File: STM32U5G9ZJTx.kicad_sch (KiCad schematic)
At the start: 42 parts, among them J1 Conn_ST_STDC14, SW1 SW_Push, SW2 SW_Push, U1 STM32U5G9ZJTxQ, Y1 16MHz, Y2 32.768KHz

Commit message: layouting component to PCB
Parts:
- C1, C10, C11, C14, C16, C18, C19, C2, C20, C21, C23, C24, C25, C26, C29, C3, C30, C31, C32, C33, C4, C5, C6, C7, C8, C9: footprint (none) -> Capacitor_SMD:C_0402_1005Metric
- C12, C13, C15, C17, C22, C27, C28: footprint (none) -> Capacitor_SMD:C_0603_1608Metric
- J1: footprint (none) -> Connector_PinHeader_1.27mm:PinHeader_2x07_P1.27mm_Vertical_SMD
- L1: footprint (none) -> Inductor_SMD:L_0603_1608Metric
- R1: footprint (none) -> Resistor_SMD:R_0402_1005Metric
- SW1, SW2: footprint (none) -> Button_Switch_SMD:SW_SPST_PTS810
- Y1: footprint (none) -> Crystal:Crystal_SMD_2520-4Pin_2.5x2.0mm
- Y2: footprint (none) -> Crystal:Crystal_SMD_2012-2Pin_2.0x1.2mm
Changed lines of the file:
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@@
 		(polyline
 			(pts
-				(xy 240.03 144.78) (xy 265.43 144.78) (xy 265.43 119.38) (xy 240.03 119.38)
+				(xy 299.72 203.2) (xy 299.72 224.79) (xy 316.23 224.79) (xy 316.23 203.2)
 			)
 			(stroke
@@
 		(polyline
 			(pts
-				(xy 364.49 119.38) (xy 364.49 144.78) (xy 400.05 144.78) (xy 400.05 119.38)
+				(xy 293.37 154.94) (xy 341.63 154.94) (xy 341.63 186.69) (xy 293.37 186.69)
 			)
 			(stroke
@@
 		(polyline
 			(pts
-				(xy 240.03 78.74) (xy 381 78.74) (xy 381 52.07) (xy 240.03 52.07)
+				(xy 240.03 110.49) (xy 265.43 110.49) (xy 265.43 85.09) (xy 240.03 85.09)
 			)
 			(stroke
@@
 		(polyline
 			(pts
-				(xy 240.03 154.94) (xy 285.75 154.94) (xy 285.75 186.69) (xy 240.03 186.69)
+				(xy 364.49 119.38) (xy 364.49 144.78) (xy 400.05 144.78) (xy 400.05 119.38)
 			)
 			(stroke
@@
 		(polyline
 			(pts
-				(xy 240.03 110.49) (xy 265.43 110.49) (xy 265.43 85.09) (xy 240.03 85.09)
+				(xy 313.69 119.38) (xy 313.69 144.78) (xy 360.68 144.78) (xy 360.68 119.38)
 			)
 			(stroke
@@
 		(polyline
 			(pts
-				(xy 358.14 110.49) (xy 386.08 110.49) (xy 386.08 85.09) (xy 358.14 85.09)
+				(xy 240.03 154.94) (xy 285.75 154.94) (xy 285.75 186.69) (xy 240.03 186.69)
 			)
 			(stroke
@@
 		(polyline
 			(pts
-				(xy 299.72 203.2) (xy 299.72 224.79) (xy 316.23 224.79) (xy 316.23 203.2)
+				(xy 313.69 110.49) (xy 349.25 110.49) (xy 349.25 85.09) (xy 313.69 85.09)
 			)
 			(stroke
@@
 		(polyline
 			(pts
-				(xy 313.69 119.38) (xy 313.69 144.78) (xy 360.68 144.78) (xy 360.68 119.38)
+				(xy 240.03 44.45) (xy 276.86 44.45) (xy 276.86 16.51) (xy 240.03 16.51)
 			)
 			(stroke
@@
 		(polyline
 			(pts
-				(xy 274.32 110.49) (xy 304.8 110.49) (xy 304.8 85.09) (xy 274.32 85.09)
+				(xy 304.8 144.78) (xy 304.8 119.38) (xy 274.32 119.38) (xy 274.32 144.78)
 			)
 			(stroke
@@
 		(polyline
 			(pts
-				(xy 304.8 144.78) (xy 304.8 119.38) (xy 274.32 119.38) (xy 274.32 144.78)
+				(xy 274.32 110.49) (xy 304.8 110.49) (xy 304.8 85.09) (xy 274.32 85.09)
 			)
 			(stroke
@@
 		(polyline
 			(pts
-				(xy 313.69 110.49) (xy 349.25 110.49) (xy 349.25 85.09) (xy 313.69 85.09)
+				(xy 240.03 78.74) (xy 381 78.74) (xy 381 52.07) (xy 240.03 52.07)
 			)
 			(stroke
@@
 		(polyline
 			(pts
-				(xy 293.37 154.94) (xy 341.63 154.94) (xy 341.63 186.69) (xy 293.37 186.69)
+				(xy 240.03 144.78) (xy 265.43 144.78) (xy 265.43 119.38) (xy 240.03 119.38)
 			)
 			(stroke
@@
 		(polyline
 			(pts
-				(xy 240.03 44.45) (xy 276.86 44.45) (xy 276.86 16.51) (xy 240.03 16.51)
+				(xy 358.14 110.49) (xy 386.08 110.49) (xy 386.08 85.09) (xy 358.14 85.09)
 			)
 			(stroke
@@
 			)
 		)
-		(property "Footprint" ""
+		(property "Footprint" "Capacitor_SMD:C_0402_1005Metric"
 			(at 257.81 173.99 0)
 			(effects
@@
 			)
 		)
-		(property "Footprint" ""
+		(property "Footprint" "Capacitor_SMD:C_0402_1005Metric"
 			(at 256.54 132.08 0)
 			(effects
@@
 			)
 		)
-		(property "Footprint" ""
+		(property "Footprint" "Capacitor_SMD:C_0603_1608Metric"
 			(at 321.0052 101.6 0)
 			(effects
@@
 			)
 		)
-		(property "Footprint" ""
+		(property "Footprint" "Capacitor_SMD:C_0603_1608Metric"
 			(at 246.0752 69.85 0)
 			(effects
@@
 			)
 		)
-		(property "Footprint" ""
+		(property "Footprint" "Button_Switch_SMD:SW_SPST_PTS810"
 			(at 367.03 201.93 0)
 			(effects
@@
 			)
 		)
-		(property "Footprint" ""
+		(property "Footprint" "Capacitor_SMD:C_0603_1608Metric"
 			(at 338.7852 137.16 0)
 			(effects
@@
 			)
 		)
-		(property "Footprint" ""
+		(property "Footprint" "Inductor_SMD:L_0603_1608Metric"
 			(at 328.93 128.27 0)
 			(effects
@@
 			)
 		)
-		(property "Footprint" ""
+		(property "Footprint" "Capacitor_SMD:C_0402_1005Metric"
 			(at 279.4 66.04 0)
 			(effects
@@
 			)
 		)
-		(property "Footprint" ""
+		(property "Footprint" "Capacitor_SMD:C_0402_1005Metric"
 			(at 267.97 31.75 0)
 			(effects
@@
 			)
 		)
-		(property "Footprint" ""
+		(property "Footprint" "Capacitor_SMD:C_0603_1608Metric"
 			(at 351.4852 137.16 0)
 			(effects
@@
 			)
 		)
-		(property "Footprint" ""
+		(property "Footprint" "Capacitor_SMD:C_0402_1005Metric"
 			(at 306.07 212.09 0)
 			(effects
@@
 			)
 		)
-		(property "Footprint" ""
+		(property "Footprint" "Capacitor_SMD:C_0402_1005Metric"
 			(at 302.26 66.04 0)
 			(effects
@@
 			)
 		)
-		(property "Footprint" ""
+		(property "Footprint" "Resistor_SMD:R_0402_1005Metric"
 			(at 359.41 213.36 0)
 			(effects
@@
 			)
 		)
-		(property "Footprint" ""
+		(property "Footprint" "Capacitor_SMD:C_0603_1608Metric"
 			(at 246.0752 35.56 0)
 			(effects
@@
 			)
 		)
-		(property "Footprint" ""
+		(property "Footprint" "Crystal:Crystal_SMD_2012-2Pin_2.0x1.2mm"
 			(at 317.5 167.64 0)
 			(effects
@@
 			)
 		)
-		(property "Footprint" ""
+		(property "Footprint" "Capacitor_SMD:C_0402_1005Metric"
 			(at 336.55 66.04 0)
 			(effects
@@
 			)
 		)
-		(property "Footprint" ""
+		(property "Footprint" "Capacitor_SMD:C_0402_1005Metric"
 			(at 382.27 133.35 0)
 			(effects
@@
 			)
 		)
-		(property "Footprint" ""
+		(property "Footprint" "Capacitor_SMD:C_0402_1005Metric"
 			(at 290.83 66.04 0)
 			(effects
@@
 			)
 		)
-		(property "Footprint" ""
+		(property "Footprint" "Capacitor_SMD:C_0402_1005Metric"
 			(at 313.69 66.04 0)
 			(effects
@@
 			)
 		)
-		(property "Footprint" ""
+		(property "Footprint" "Capacitor_SMD:C_0603_1608Metric"
 			(at 280.3652 137.16 0)
 			(effects
@@
 			)
 		)
-		(property "Footprint" ""
+		(property "Footprint" "Capacitor_SMD:C_0402_1005Metric"
 			(at 347.98 66.04 0)
 			(effects
@@
 			)
 		)
-		(property "Footprint" ""
+		(property "Footprint" "Capacitor_SMD:C_0402_1005Metric"
 			(at 256.54 66.04 0)
 			(effects
@@
 			)
 		)
-		(property "Footprint" ""
+		(property "Footprint" "Connector_PinHeader_1.27mm:PinHeader_2x07_P1.27mm_Vertical_SMD"
 			(at 270.51 219.71 0)
 			(effects
@@
 			)
 		)
-		(property "Footprint" ""
+		(property "Footprint" "Capacitor_SMD:C_0402_1005Metric"
 			(at 245.11 97.79 0)
 			(effects
@@
 			)
 		)
-		(property "Footprint" ""
+		(property "Footprint" "Capacitor_SMD:C_0402_1005Metric"
 			(at 322.58 171.45 0)
 			(effects
@@
 			)
 		)
-		(property "Footprint" ""
+		(property "Footprint" "Capacitor_SMD:C_0402_1005Metric"
 			(at 370.84 133.35 0)
 			(effects
@@
 			)
 		)
-		(property "Footprint" ""
+		(property "Footprint" "Capacitor_SMD:C_0402_1005Metric"
 			(at 267.97 173.99 0)
 			(effects
@@
 			)
 		)
-		(property "Footprint" ""
+		(property "Footprint" "Capacitor_SMD:C_0402_1005Metric"
 			(at 290.83 133.35 0)
 			(effects
@@
 			)
 		)
-		(property "Footprint" ""
+		(property "Footprint" "Capacitor_SMD:C_0402_1005Metric"
 			(at 256.54 31.75 0)
 			(effects
@@
 			)
 		)
-		(property "Footprint" ""
+		(property "Footprint" "Capacitor_SMD:C_0402_1005Metric"
 			(at 331.47 97.79 0)
 			(effects
@@
 			)
 		)
-		(property "Footprint" ""
+		(property "Footprint" "Capacitor_SMD:C_0402_1005Metric"
 			(at 267.97 66.04 0)
 			(effects
@@
 			)
 		)
-		(property "Footprint" ""
+		(property "Footprint" "Capacitor_SMD:C_0402_1005Metric"
 			(at 359.41 66.04 0)
 			(effects
@@
 			)
 		)
-		(property "Footprint" ""
+		(property "Footprint" "Capacitor_SMD:C_0402_1005Metric"
 			(at 325.12 66.04 0)
 			(effects
@@
 			)
 		)
-		(property "Footprint" ""
+		(property "Footprint" "Capacitor_SMD:C_0402_1005Metric"
 			(at 363.22 97.79 0)
 			(effects
@@
 			)
 		)
-		(property "Footprint" ""
+		(property "Footprint" "Crystal:Crystal_SMD_2520-4Pin_2.5x2.0mm"
 			(at 262.89 167.64 0)
 			(effects
@@
 			)
 		)
-		(property "Footprint" ""
+		(property "Footprint" "Capacitor_SMD:C_0402_1005Metric"
 			(at 370.84 66.04 0)
 			(effects
@@
 			)
 		)
-		(property "Footprint" ""
+		(property "Footprint" "Capacitor_SMD:C_0402_1005Metric"
 			(at 312.42 171.45 0)
 			(effects
@@
 			)
 		)
-		(property "Footprint" ""
+		(property "Footprint" "Capacitor_SMD:C_0402_1005Metric"
 			(at 279.4 97.79 0)
 			(effects
@@
 			)
 		)
-		(property "Footprint" ""
+		(property "Footprint" "Capacitor_SMD:C_0603_1608Metric"
 			(at 246.0752 135.89 0)
 			(effects
@@
 			)
 		)
-		(property "Footprint" ""
+		(property "Footprint" "Button_Switch_SMD:SW_SPST_PTS810"
 			(at 335.28 201.93 0)
 			(effects

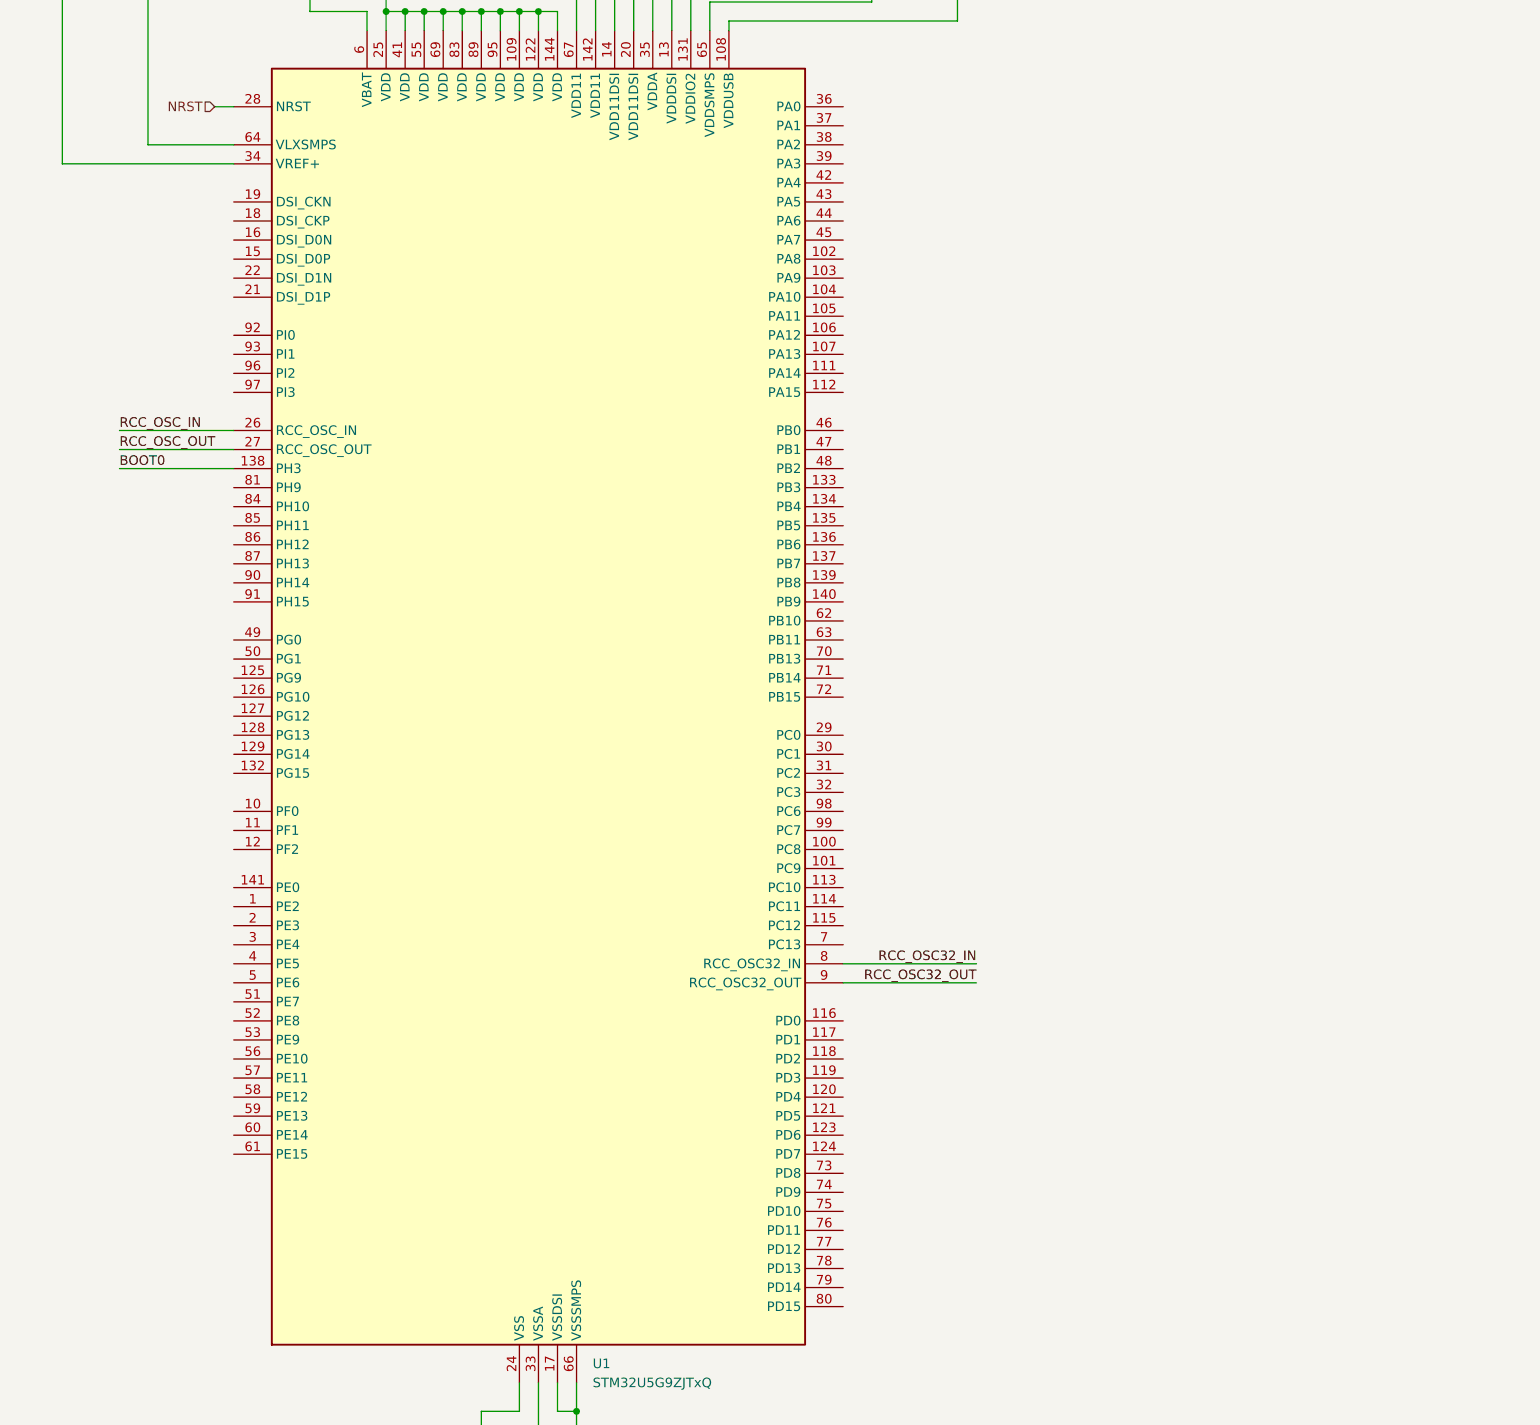
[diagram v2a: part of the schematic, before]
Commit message: Add connection from OSPI Flash and LCD to MCU
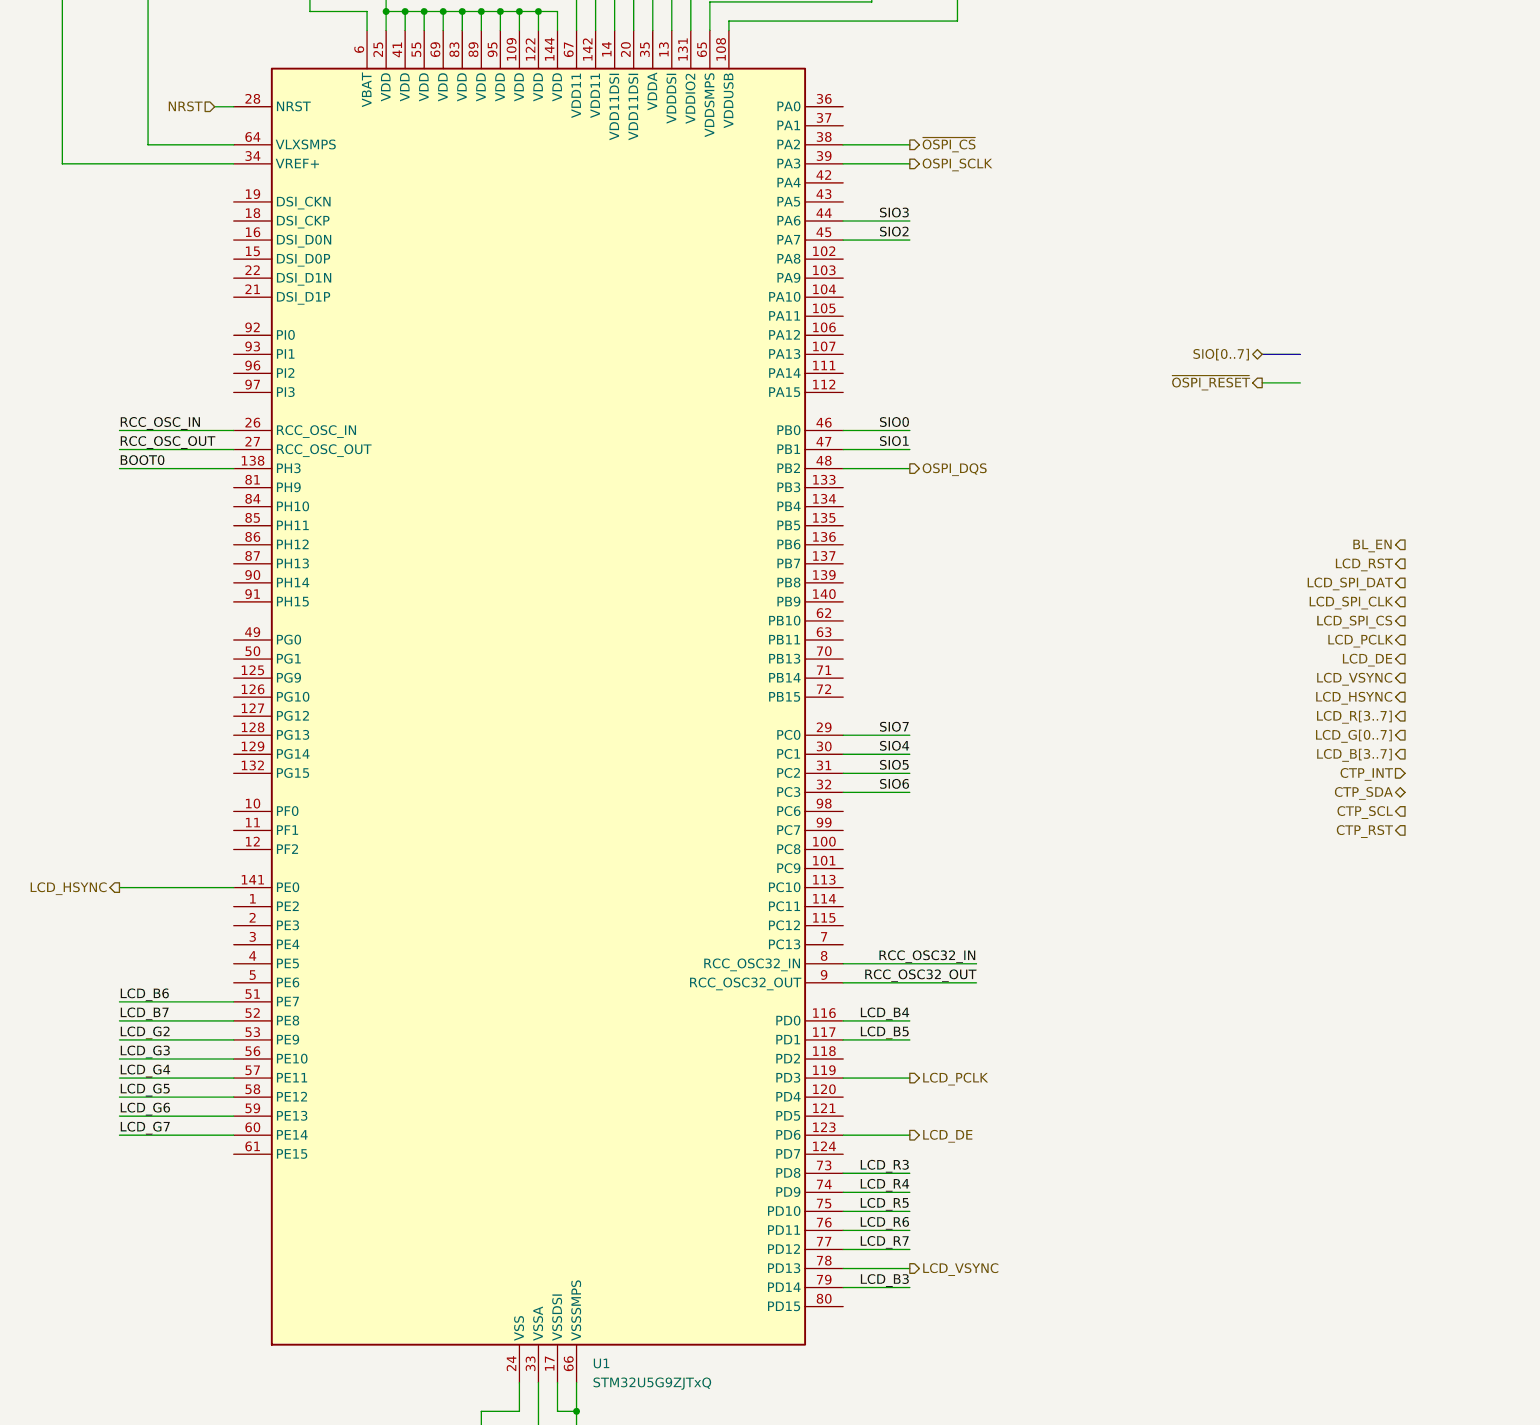
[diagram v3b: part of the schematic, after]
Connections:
- net LCD_B4: now reaches U1.116 (PD0)
- net LCD_B5: now reaches U1.117 (PD1)
- net LCD_PCLK: now reaches U1.119 (PD3)
- net LCD_DE: now reaches U1.123 (PD6)
- net LCD_HSYNC: now reaches U1.141 (PE0)
- net SIO7: now reaches U1.29 (PC0)
- net SIO4: now reaches U1.30 (PC1)
- net SIO5: now reaches U1.31 (PC2)
- net SIO6: now reaches U1.32 (PC3)
- net ~{OSPI_CS}: now reaches U1.38 (PA2)
- net OSPI_SCLK: now reaches U1.39 (PA3)
- net SIO3: now reaches U1.44 (PA6)
- net SIO2: now reaches U1.45 (PA7)
- net SIO0: now reaches U1.46 (PB0)
- net SIO1: now reaches U1.47 (PB1)
- net OSPI_DQS: now reaches U1.48 (PB2)
- net LCD_B6: now reaches U1.51 (PE7)
- net LCD_B7: now reaches U1.52 (PE8)
- net LCD_G2: now reaches U1.53 (PE9)
- net LCD_G3: now reaches U1.56 (PE10)
- net LCD_G4: now reaches U1.57 (PE11)
- net LCD_G5: now reaches U1.58 (PE12)
- net LCD_G6: now reaches U1.59 (PE13)
- net LCD_G7: now reaches U1.60 (PE14)
- net LCD_R3: now reaches U1.73 (PD8)
- net LCD_R4: now reaches U1.74 (PD9)
- net LCD_R5: now reaches U1.75 (PD10)
- net LCD_R6: now reaches U1.76 (PD11)
- net LCD_R7: now reaches U1.77 (PD12)
- net LCD_VSYNC: now reaches U1.78 (PD13)
- net LCD_B3: now reaches U1.79 (PD14)
